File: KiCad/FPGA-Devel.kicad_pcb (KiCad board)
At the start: 4 copper layers, 100 x 80 mm, 228 parts, among them J1001 Micro_SD_Card_Det1, J401 Conn_02x06_Top_Bottom, J402 Conn_02x06_Top_Bottom, J403 Conn_02x06_Top_Bottom, J404 USB_C_Receptacle_USB2.0_16P, J405 Conn_01x02_Pin, J801 USB_C_Receptacle_USB2.0_16P, Q201 BC847W, Q401 BC857W, Q402 BC857W, Q403 BC857W, Q404 BC857W, Q405 BC857W, SW401 SW_DIP_x04, SW402 SW_DIP_x04, SW403 SW_Omron_B3FS, SW404 SW_Omron_B3FS, SW405 SW_Omron_B3FS, SW406 SW_Omron_B3FS, SW407 SW_Omron_B3FS, SW408 SW_Omron_B3FS, SW409 SW_Omron_B3FS, SW410 SW_Omron_B3FS, SW411 SW_Omron_B3FS, SW412 RotaryEncoder_Switch, SW413 RKJXV1224, SW501 SW_Omron_B3FS, U1001 IS25LP032D-JNLE, U1002 APS6404, U201 TLV62568DDC, U202 TLV62568DDC, U203 TLV62568DDC, U401 LTC-4627JR, U502 XC7S50FTGB196, U801 FT2232HQ, U802 93LCxxB, U901 LM2903, X401 100MHz, Y801 12MHz

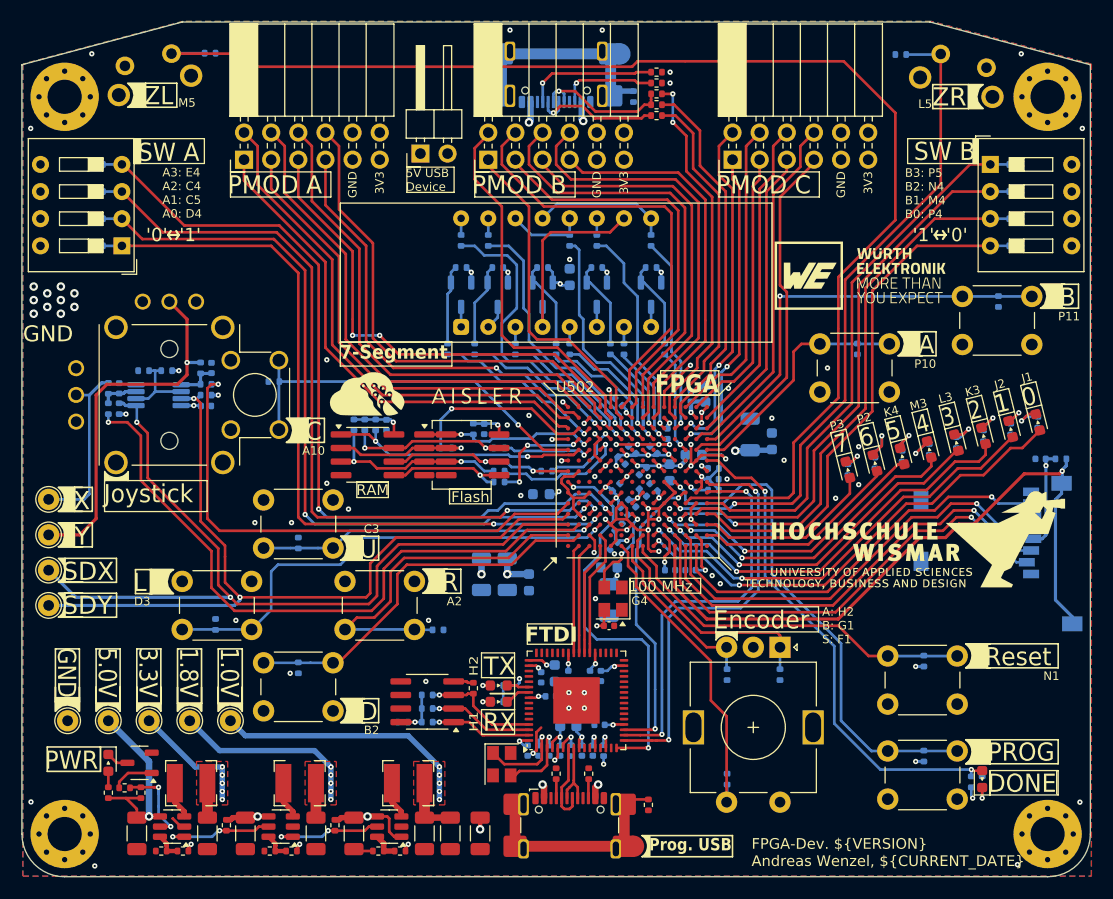
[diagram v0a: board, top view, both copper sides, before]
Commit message: Pinout und Silkscreen angepasst
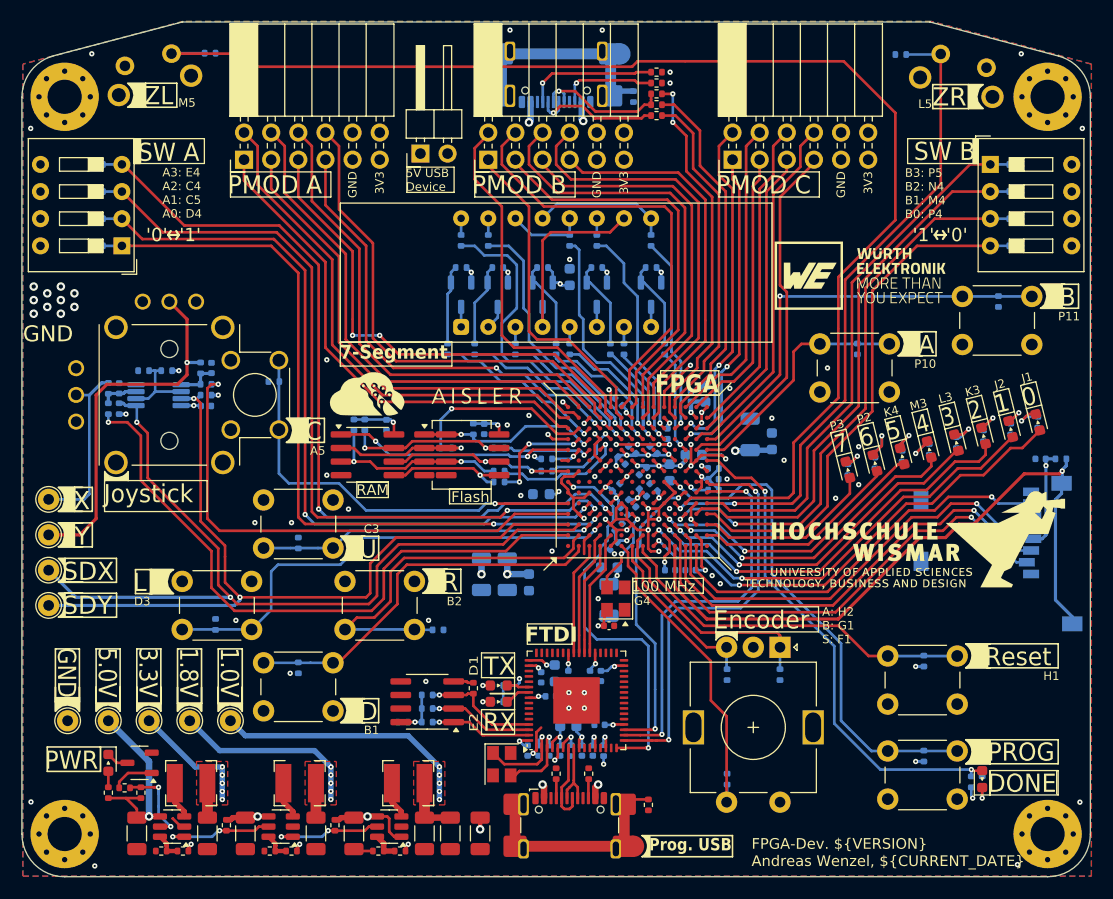
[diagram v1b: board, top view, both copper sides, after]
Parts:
- moved R601 16.3 mm to (88.0, 99.9), turned to 180 degrees
- moved X401 0.25 mm to (94.5, 113.0)
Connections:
- R601 pad 1: /Memory/SPI_Mem.CS1 -> Net-(U502A-IO_L3P_T0_DQS_PUDC_B_14)
- U502 pad A10: /IO/Btn.C -> /Memory/SPI_Mem.CS1
- U502 pad A2: /IO/Btn.R -> /ADC/ADC.FB_out0
- U502 pad A3: /ADC/ADC.SD_in0 -> /ADC/ADC.SD_in1
- U502 pad A4: /ADC/ADC.SD_in1 -> /ADC/ADC.FB_out1
- U502 pad A5: /ADC/ADC.FB_out1 -> /IO/Btn.C
- U502 pad B1: /FT2232/UART.CTS -> /IO/Btn.D
- U502 pad B10: /Memory/SPI_Mem.CS1 -> Net-(U502A-IO_L3P_T0_DQS_PUDC_B_14)
- U502 pad B2: /IO/Btn.D -> /IO/Btn.R
- U502 pad B3: /ADC/ADC.FB_out0 -> /ADC/ADC.SD_in0
- U502 pad C1: /FT2232/UART.RTS -> /FT2232/UART.CTS
- U502 pad D2: /FT2232/UART.RX -> /FT2232/UART.RTS
- U502 pad E2: unconnected-(U502B-IO_L10P_T1_34-PadE2) -> /FT2232/UART.RX
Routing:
- net /IO/Btn.C: track 36.2 -> 39.4 mm
- net Net-(U502A-IO_L3P_T0_DQS_PUDC_B_14): track 0.00 -> 2.92 mm, vias 0 -> 1
- net /Memory/SPI_Mem.CS1: track 24.9 -> 22.4 mm
- net /IO/Btn.R: track 34.5 -> 35.9 mm
- net /FT2232/UART.RTS: track 10.4 -> 11.8 mm
- net /ADC/ADC.FB_out0: track 61.5 -> 60.1 mm
- net /ADC/ADC.SD_in0: track 77.9 -> 78.9 mm
- net Net-(U502C-PROGRAM_B_0): track 47.6 -> 46.8 mm
- net GND: track 77.3 -> 77.9 mm, vias 83 -> 82
- net +3.3V: track 100.1 -> 100.7 mm, vias 39 -> 40
- net /Memory/SPI_Mem.CS0: track 16.9 -> 17.4 mm
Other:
- outline, holes or cut-outs redrawn
- board text added: "1000 100 10 1 Dots"
- board text added: "15"
- board text added: "25"
- board text added: "50"
- board text added: "7-Segment AN AN AN AN AN"
- board text added: "A3 A4"
- board text added: "A5"
- board text added: "B1"
- board text added: "B3 A2"
- board text added: "D1"
- board text added: "E11 B11 B12 D10 C10 C11 A10"
- board text added: "E2"
- board text added: "E2 D1 D2 C1"
- board text added: "XC7S FTGB196-1"
- board text removed: "7-Segment AN1 AN2 AN3 AN4 AN5"
- board text removed: "A10"
- board text removed: "A2"
- board text removed: "A3 A2"
- board text removed: "A4 A5"
- board text removed: "D2 D1 C1 B1"
- board text removed: "E11 B11 B12 D10 C10 C11 B10"
- board text removed: "H2"
- board text removed: "N1"

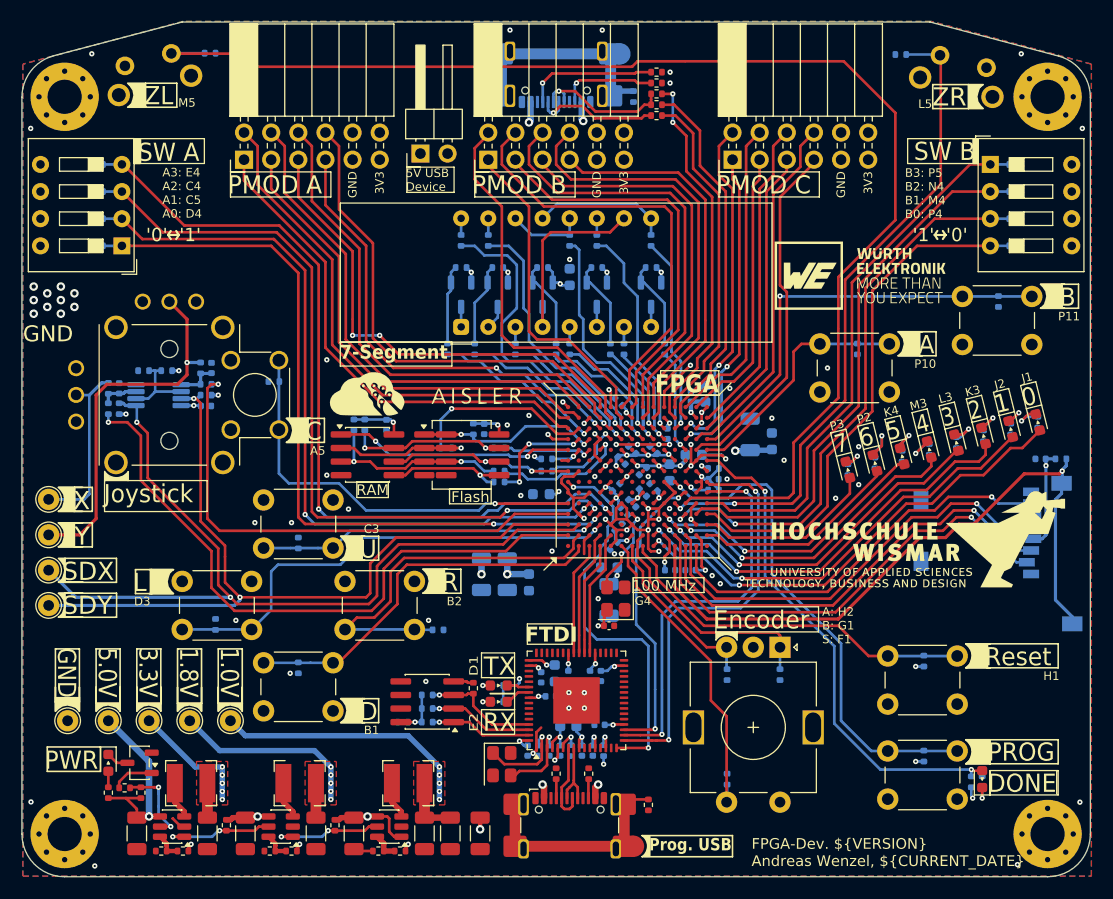
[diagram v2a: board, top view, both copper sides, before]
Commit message: Step-Files angepasst, Logo hinzugefügt
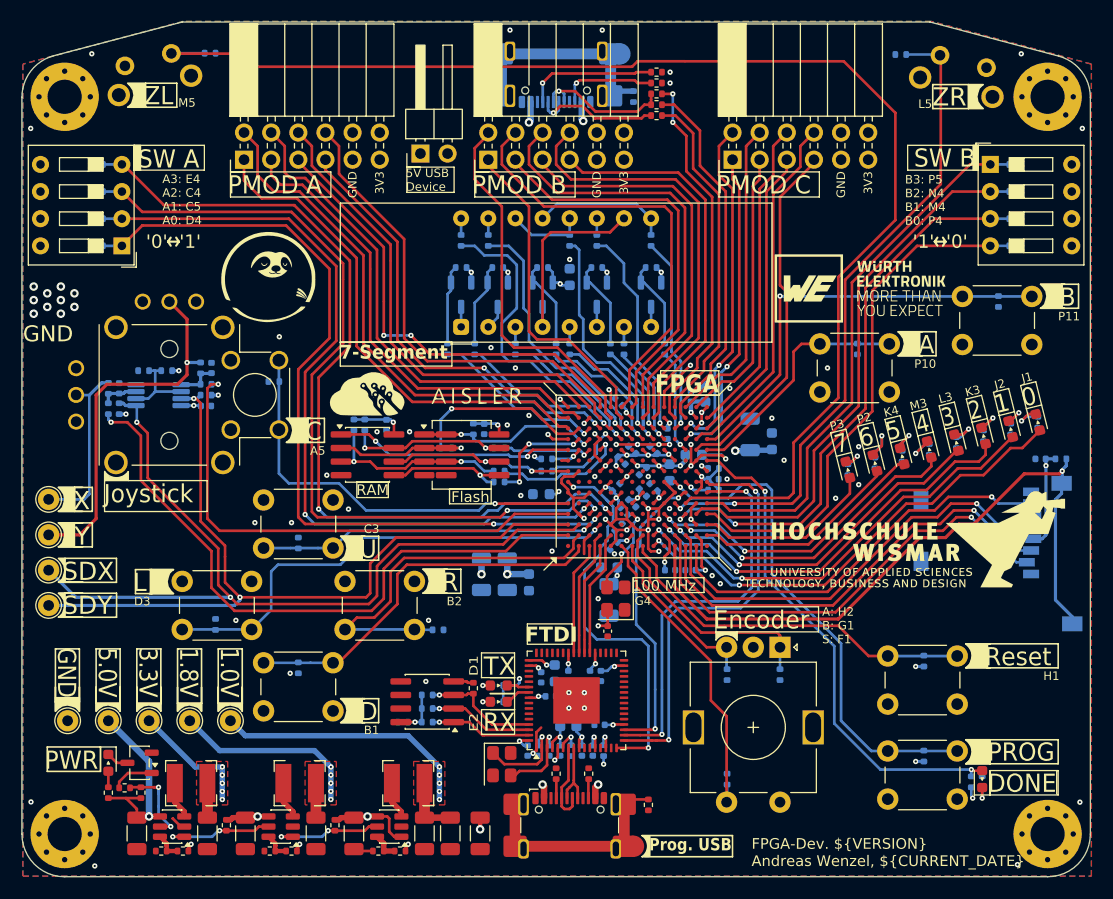
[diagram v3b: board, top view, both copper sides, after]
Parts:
- added REF**: Unbenannt, Library:Logo_Sloth, F.Cu at (62.0, 82.8)
- moved G*** 1.20 mm to (117.4, 84.0)
- moved C402 0.52 mm to (93.7, 116.1), turned to -90 degrees
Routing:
- net /IO/SW.A0: track 71.1 -> 77.0 mm
- net /IO/SW.A3: track 76.3 -> 80.6 mm
- net /IO/SW.A2: track 73.7 -> 78.1 mm
- net /IO/SW.A1: track 71.9 -> 76.3 mm
- net /Connectors/PMOD.A7: track 46.1 -> 44.3 mm
- net /Connectors/PMOD.A4: track 43.8 -> 42.1 mm
- net /Connectors/PMOD.A8: track 45.9 -> 44.2 mm
- net /Connectors/PMOD.A3: track 44.9 -> 43.2 mm
- net /Connectors/PMOD.A6: track 46.8 -> 45.8 mm
- net /Connectors/PMOD.A2: track 45.1 -> 44.5 mm
- net GND: track 77.9 -> 78.3 mm, vias 82 -> 86
